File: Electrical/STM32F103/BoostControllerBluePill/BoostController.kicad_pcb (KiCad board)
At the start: 2 copper layers, 81.8 x 80 mm, 66 parts, among them J1 PW-RPM-SPD-TPS, J2 OIL-WATER-AFR, J3 WG-FPUMP, J4 MAP-FPRES, J5 CAN, J6 GND_TP, J7 PROG, J8 SERIAL, Q1 IRF3205, Q2 IRF3205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

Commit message: Added CAN load resistor and jumper
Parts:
- added JP1: CAN load resistor, Connector_PinHeader_2.54mm:PinHeader_1x02_P2.54mm_Vertical, F.Cu at (129.3, 108.7)
- added R25: 120, Resistor_SMD:R_1206_3216Metric_Pad1.30x1.75mm_HandSolder, B.Cu at (132.8, 99.6)
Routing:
- net Net-(JP1-Pad2): track 0.00 -> 10.1 mm
- net /CANL: track 13.3 -> 17.7 mm

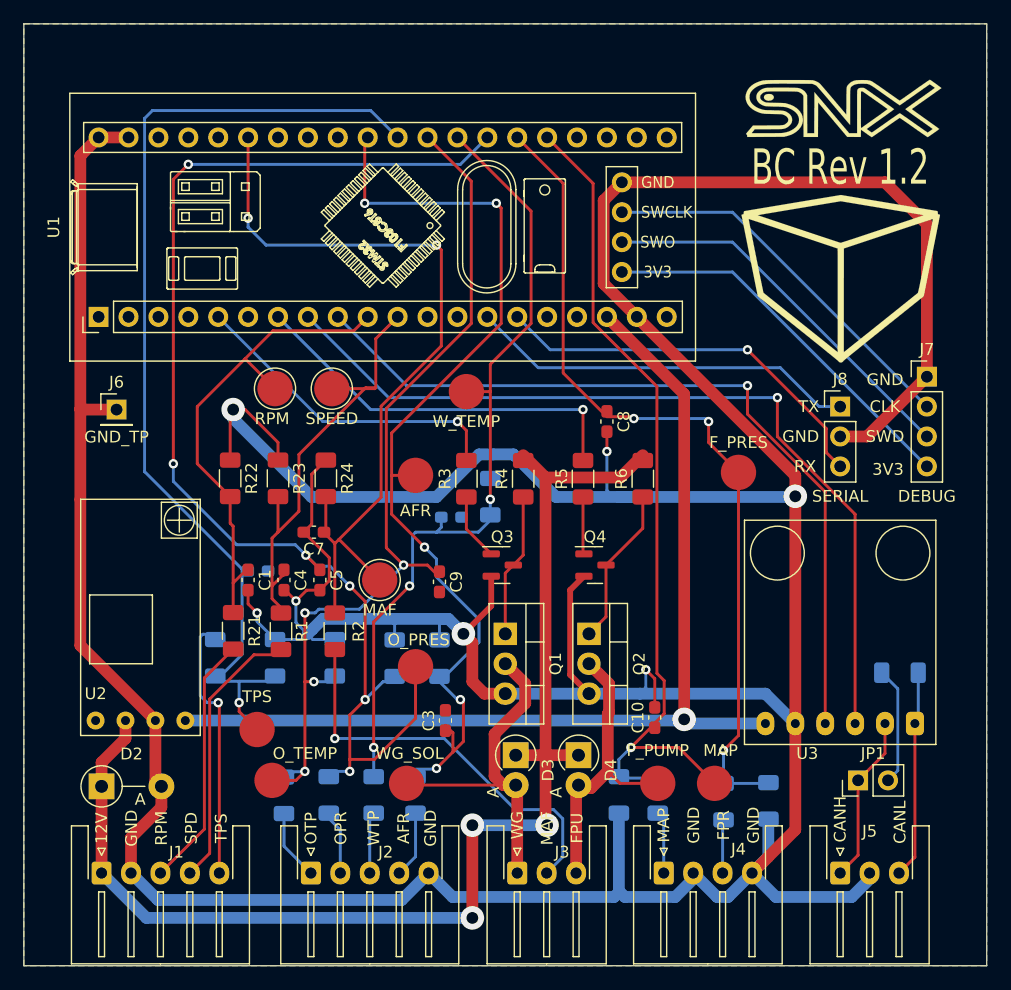
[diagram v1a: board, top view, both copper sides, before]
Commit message: Added OP Amp on analog inputs Split schematics with sub schematic for analog inputs.
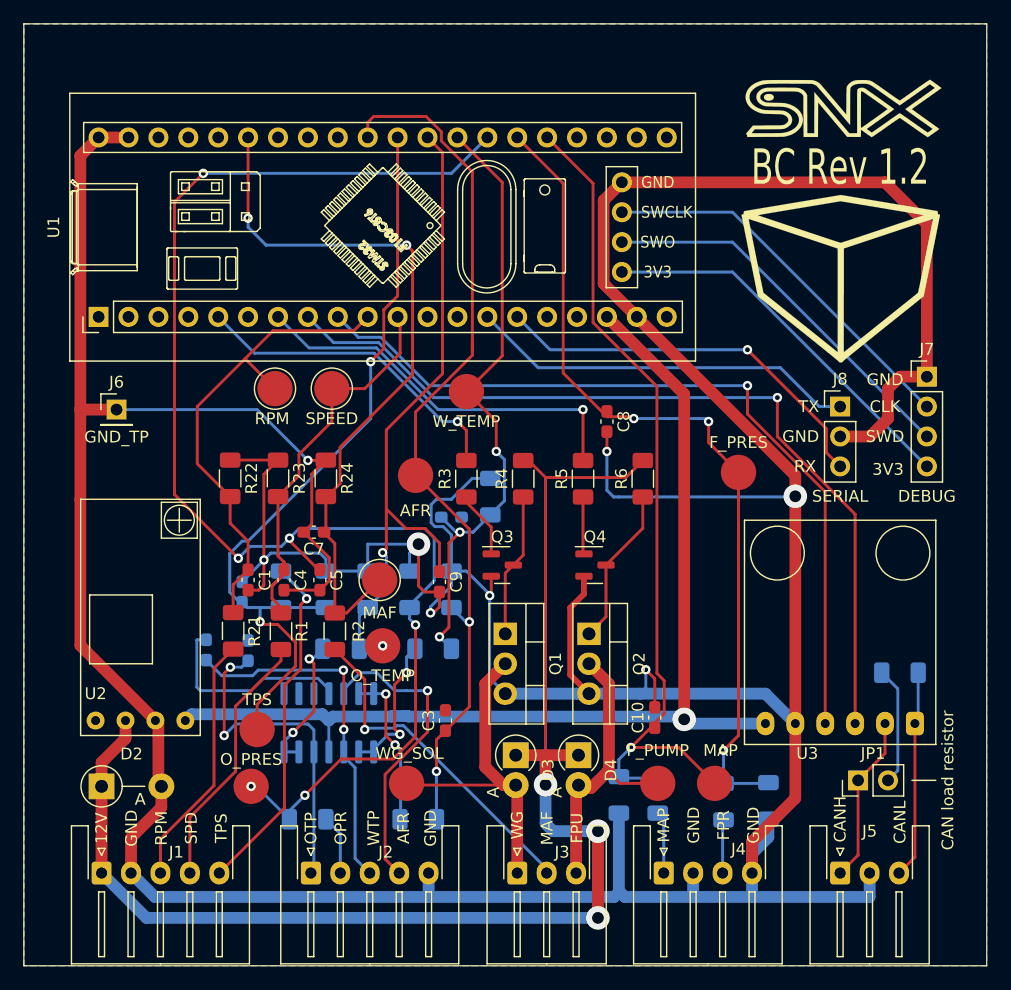
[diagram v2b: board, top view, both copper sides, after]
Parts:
- added C11: 10µ, Capacitor_SMD:C_0603_1608Metric_Pad1.08x0.95mm_HandSolder, B.Cu at (73.9, 97.6)
- added C12: 10µ, Capacitor_SMD:C_0603_1608Metric_Pad1.08x0.95mm_HandSolder, B.Cu at (77.5, 97.7)
- added U4: LM324, Package_SO:SO-14_3.9x8.65mm_P1.27mm, B.Cu at (84.3, 103.8)
- moved TP5 17.3 mm to (77.7, 109.2)
- moved TP8 14.8 mm to (88.9, 97.3)
- moved R7 13.4 mm to (93.2, 97.5), turned to 0 degrees
- moved R17 13.4 mm to (85.4, 97.5), turned to 0 degrees
- moved R13 8.07 mm to (80.3, 92.5)
- moved R14 7.24 mm to (84.1, 92.5)
- moved R18 6.45 mm to (87.6, 92.5)
- moved R12 5.98 mm to (91.2, 92.5)
- moved R10 5.94 mm to (94.7, 92.5)
- moved R11 2.74 mm to (82.5, 112.0), turned to 180 degrees
- moved C6 2.23 mm to (77.0, 92.7), turned to 90 degrees
- moved R9 2.08 mm to (91.9, 112.0), turned to 0 degrees
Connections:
- net /AFR_33 renamed AFR_33
- net /F_PRES renamed F_PRES
- net /F_PRES_33 renamed F_PRES_33
- net /MAP renamed MAP
- net /MAP_33 renamed MAP_33
- net /OIL_PRES renamed OIL_PRES
- net /OIL_PRES_33 renamed OIL_PRES_33
- net /OIL_TEMP_33 renamed OIL_TEMP_33
- net /TPS renamed TPS
- net /TPS_33 renamed TPS_33
- net /WATER_TEMP_33 renamed WATER_TEMP_33
- J2 pad 1: /OIL_TEMP -> OIL_TEMP
- J2 pad 3: /WATER_TEMP -> WATER_TEMP
- J2 pad 4: /AFR -> AFR
- R17 pad 1: /OIL_TEMP -> Net-(R17-Pad1)
- R7 pad 1: /WATER_TEMP -> Net-(R7-Pad1)
- R9 pad 1: /AFR -> Net-(R9-Pad1)
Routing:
- net WATER_TEMP: track 0.00 -> 30.6 mm, vias 0 -> 2
- net OIL_TEMP: track 0.00 -> 28.3 mm, vias 0 -> 2
- net AFR: track 0.00 -> 26.2 mm, vias 0 -> 1
- net OIL_TEMP_33: track 75.9 -> 57.5 mm, vias 4 -> 2
- net GND: track 452.2 -> 470.5 mm, vias 7 -> 8
- net TPS_33: track 84.7 -> 67.3 mm, vias 1 -> 2
- net WATER_TEMP_33: track 68.4 -> 53.1 mm
- net Net-(R9-Pad1): track 0.00 -> 13.5 mm, vias 0 -> 2
- net Net-(R7-Pad1): track 0.00 -> 12.4 mm, vias 0 -> 2
- net OIL_PRES_33: track 107.4 -> 119.6 mm
- net Net-(R17-Pad1): track 0.00 -> 11.9 mm, vias 0 -> 2
- net +12V: track 107.8 -> 115.7 mm
- net /MAF_33: track 68.3 -> 61.2 mm
- net TPS: track 22.7 -> 29.6 mm
- net AFR_33: track 81.7 -> 75.7 mm, vias 5 -> 2
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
